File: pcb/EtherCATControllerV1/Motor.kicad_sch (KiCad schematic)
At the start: 1 part, among them U6 MCF8329A1IREER

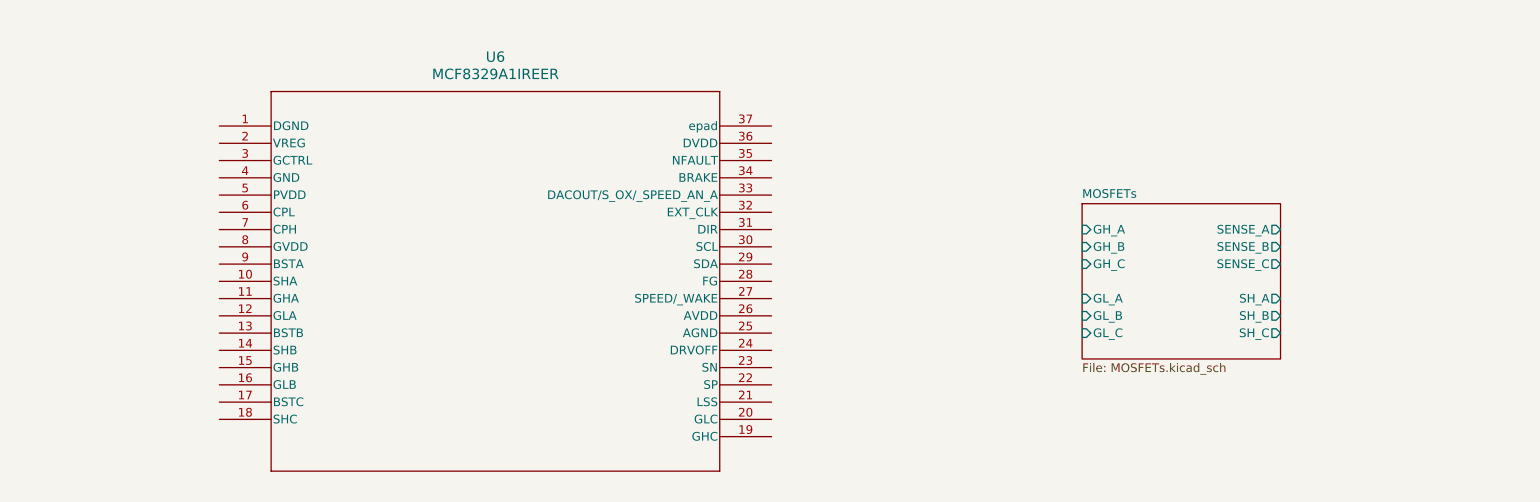
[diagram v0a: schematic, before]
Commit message: Initial design without Ethernet connectors
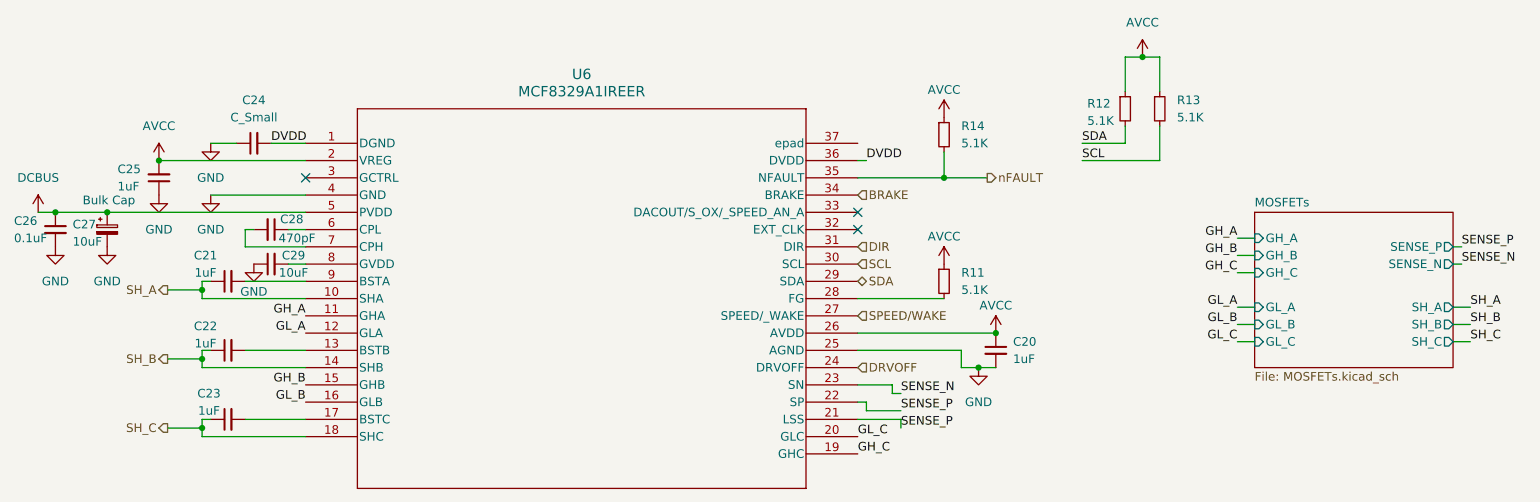
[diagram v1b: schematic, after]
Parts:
- added C20, C21, C22, C23, C25: 1uF, symbol Device:C_Small
- added C24: C_Small, symbol Device:C_Small
- added C26: 0.1uF, symbol Device:C_Small
- added C27: 10uF, symbol Device:C_Polarized_Small
- added C28: 470pF, symbol Device:C_Small
- added C29: 10uF, symbol Device:C_Small
- added R11, R12, R13, R14: 5.1K, symbol Device:R_Small
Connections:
- net DVDD: now reaches U6.1 (DGND)
- net DVDD: now also U6.36 (DVDD), C24.2
- net SH_A: now reaches U6.10 (SHA)
- net SH_A: now also C21.1
- net GH_A: now reaches U6.11 (GHA)
- net GL_A: now reaches U6.12 (GLA)
- net at U6.13 (BSTB): now also C22.2
- net SH_B: now reaches U6.14 (SHB)
- net SH_B: now also C22.1
- net GH_B: now reaches U6.15 (GHB)
- net GL_B: now reaches U6.16 (GLB)
- net at U6.17 (BSTC): now also C23.2
- net SH_C: now reaches U6.18 (SHC)
- net SH_C: now also C23.1
- net GH_C: now reaches U6.19 (GHC)
- net AVCC: now reaches U6.2 (VREG)
- net AVCC: now also U6.26 (AVDD), C20.1, C25.2, R11.1, R12.1, R13.1, R14.1
- net GL_C: now reaches U6.20 (GLC)
- net SENSE_P: now reaches U6.21 (LSS)
- net SENSE_P: now also U6.22 (SP)
- net SENSE_N: now reaches U6.23 (SN)
- net DRVOFF: now reaches U6.24 (DRVOFF)
- net GND: now reaches U6.25 (AGND)
- net GND: now also U6.4 (GND), C20.2, C24.1, C25.1, C26.2, C27.2, C29.1
- net SPEED/WAKE: now reaches U6.27 (SPEED/_WAKE)
- net at U6.28 (FG): now also R11.2
- net SDA: now reaches U6.29 (SDA)
- net SDA: now also R12.2
- net SCL: now reaches U6.30 (SCL)
- net SCL: now also R13.2
- net DIR: now reaches U6.31 (DIR)
- net BRAKE: now reaches U6.34 (BRAKE)
- net nFAULT: now reaches U6.35 (NFAULT)
- net nFAULT: now also R14.2
- net DCBUS: now reaches U6.5 (PVDD)
- net DCBUS: now also C26.1, C27.1
- net at U6.6 (CPL): now also C28.1
- net at U6.7 (CPH): now also C28.2
- net at U6.8 (GVDD): now also C29.2
- net at U6.9 (BSTA): now also C21.2
- no-connect marks 0 -> 3
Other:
- sheet MOSFETs ports: added SENSE_N, SENSE_P; removed SENSE_A, SENSE_B, SENSE_C
- note added: "Bulk Cap"

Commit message: fix all ERCs
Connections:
- net GND: now also U6.37 (epad)
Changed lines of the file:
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@@
 	(wire
 		(pts
-			(xy 151.13 111.76) (xy 157.48 111.76)
+			(xy 156.21 113.03) (xy 157.48 113.03)
 		)
 		(stroke
@@
 	(wire
 		(pts
+			(xy 156.21 111.76) (xy 151.13 111.76)
+		)
+		(stroke
+			(width 0)
+			(type default)
+		)
+	)
+	(wire
+		(pts
 			(xy 49.53 102.87) (xy 54.61 102.87)
 		)
@@
 	(wire
 		(pts
+			(xy 156.21 113.03) (xy 156.21 111.76)
+		)
+		(stroke
+			(width 0)
+			(type default)
+		)
+	)
+	(wire
+		(pts
 			(xy 55.88 101.6) (xy 54.61 101.6)
 		)
@@
 	(wire
 		(pts
-			(xy 157.48 111.76) (xy 157.48 113.03)
-		)
-		(stroke
-			(width 0)
-			(type default)
-		)
-	)
-	(wire
-		(pts
 			(xy 54.61 114.3) (xy 69.85 114.3)
 		)
@@
 		(pts
 			(xy 195.58 58.42) (xy 195.58 63.5)
+		)
+		(stroke
+			(width 0)
+			(type default)
+		)
+	)
+	(wire
+		(pts
+			(xy 151.13 71.12) (xy 160.02 71.12)
 		)
 		(stroke
@@
 	)
 	(symbol
+		(lib_id "power:GND")
+		(at 160.02 71.12 0)
+		(unit 1)
+		(exclude_from_sim no)
+		(in_bom yes)
+		(on_board yes)
+		(dnp no)
+		(property "Reference" "#PWR0111"
+			(at 160.02 77.47 0)
+			(effects
+				(font
+					(size 1.27 1.27)
+				)
+				(hide yes)
+			)
+		)
+		(property "Value" "GND"
+			(at 160.02 75.438 0)
+			(effects
+				(font
+					(size 1.27 1.27)
+				)
+			)
+		)
+		(property "Footprint" ""
+			(at 160.02 71.12 0)
+			(effects
+				(font
+					(size 1.27 1.27)
+				)
+				(hide yes)
+			)
+		)
+		(property "Datasheet" ""
+			(at 160.02 71.12 0)
+			(effects
+				(font
+					(size 1.27 1.27)
+				)
+				(hide yes)
+			)
+		)
+		(property "Description" "Power symbol creates a global label with name \"GND\" , ground"
+			(at 160.02 71.12 0)
+			(effects
+				(font
+					(size 1.27 1.27)
+				)
+				(hide yes)
+			)
+		)
+		(pin "1"
+		)
+		(instances
+			(project "EtherCATControllerV1"
+				(path "/4c927f80-855d-490a-80b2-e5c55283621a/b8886fcf-711b-4283-9745-a57e39aa3085"
+					(reference "#PWR0111")
+					(unit 1)
+				)
+			)
+		)
+	)
+	(symbol
 		(lib_id "power:VCC")
 		(at 163.83 67.31 0)
@@
 			(at 69.85 71.12 0)
 			(effects
+				(font
+					(size 1.27 1.27)
+				)
+				(hide yes)
+			)
+		)
+		(property "LCSC Part Number" ""
+			(at 69.85 71.12 0)
+			(effects
+				(font
+					(size 1.27 1.27)
+				)
+				(hide yes)
+			)
+		)
+		(property "Field-1" ""
+			(at 69.85 71.12 0)
+			(effects

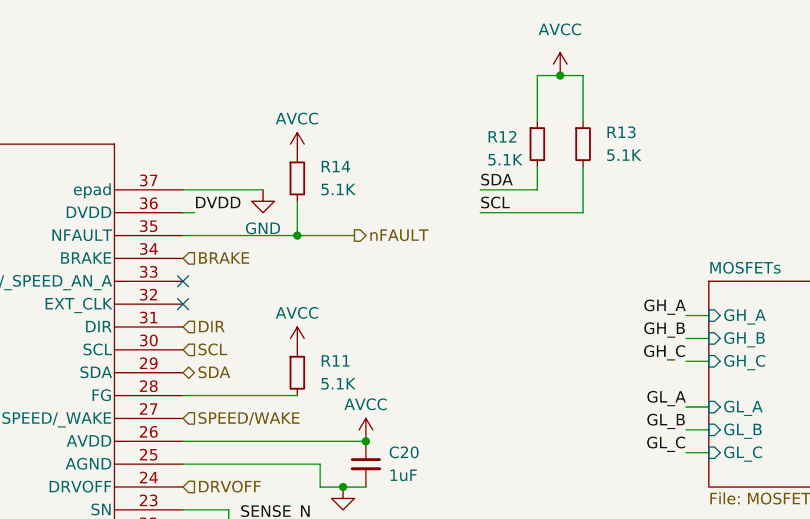
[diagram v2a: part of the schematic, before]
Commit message: Added more BOM items
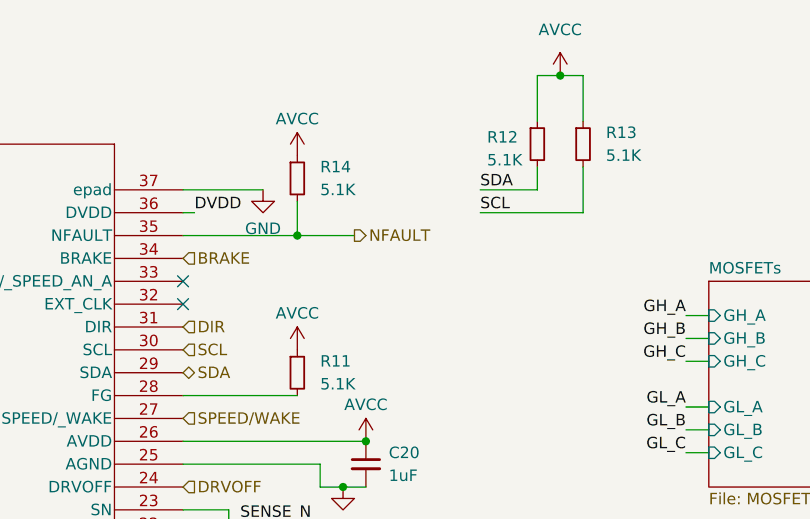
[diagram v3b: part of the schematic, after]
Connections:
- net nFAULT renamed NFAULT
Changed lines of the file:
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@@
 		)
 	)
-	(hierarchical_label "nFAULT"
+	(hierarchical_label "NFAULT"
 		(shape output)
 		(at 170.18 76.2 0)

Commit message: checkpoint
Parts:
- U6: LCSC Part Number (none) -> C22399784
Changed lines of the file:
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@@
 			)
 		)
-		(property "LCSC Part Number" ""
+		(property "LCSC Part Number" "C22399784"
 			(at 69.85 71.12 0)
 			(effects
-				(font
-					(size 1.27 1.27)
-				)
-				(hide yes)
-			)
-		)
-		(property "Field-1" ""
-			(at 69.85 71.12 0)
-			(effects
